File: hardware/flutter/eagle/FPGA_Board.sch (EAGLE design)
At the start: 38 parts, among them IC1 AT45DB161D-SU, U2 XC3S50AVQ100

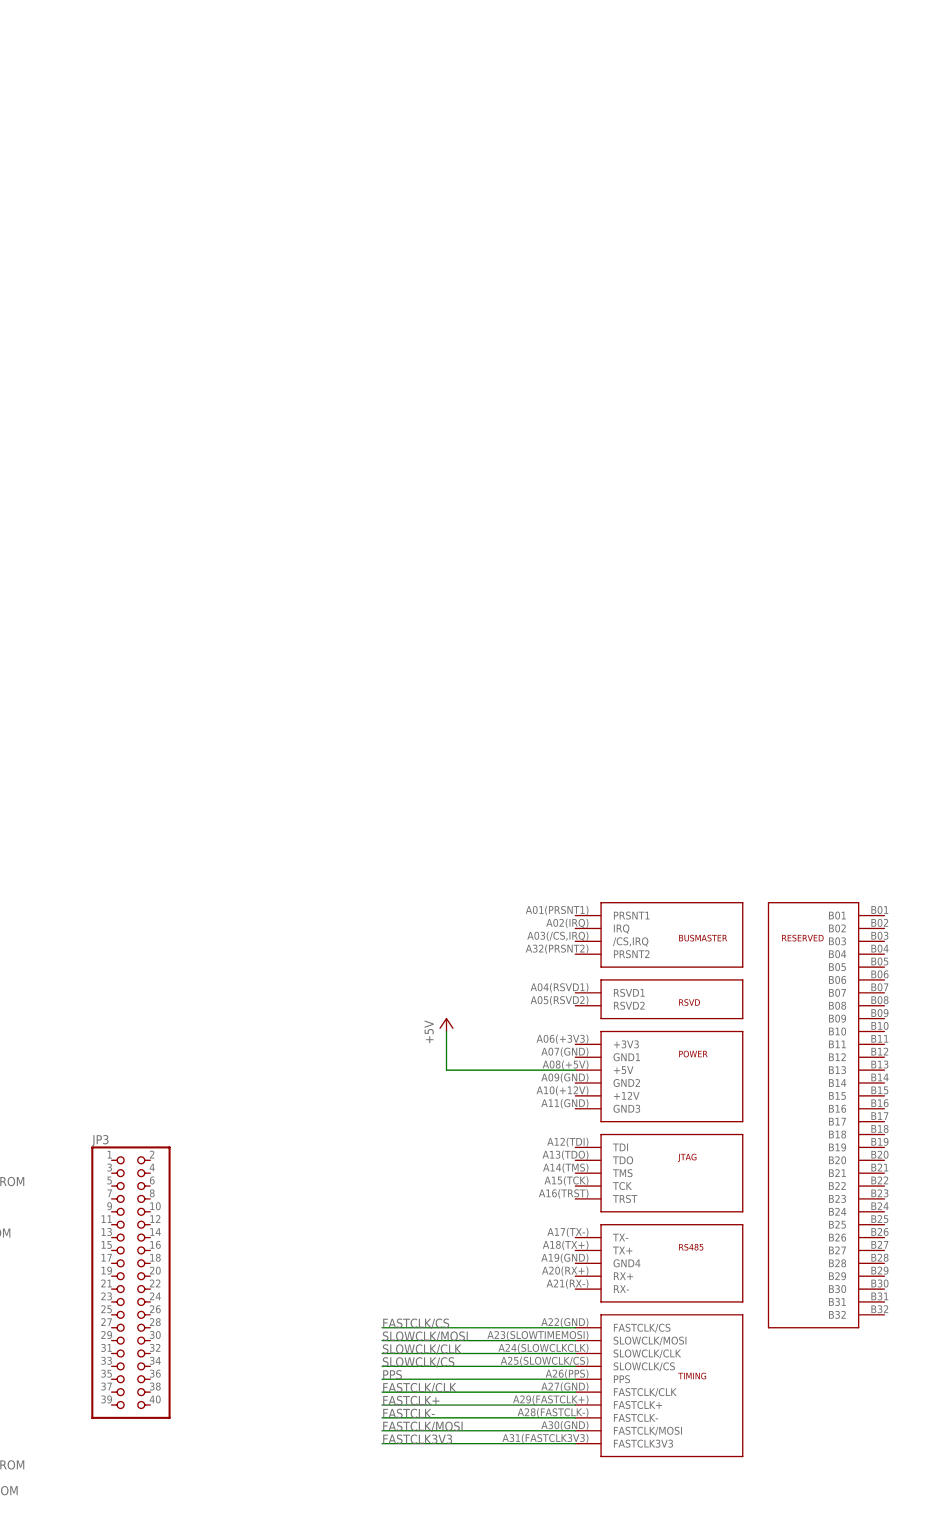
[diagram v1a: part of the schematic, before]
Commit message: added atmega8 to flutter board
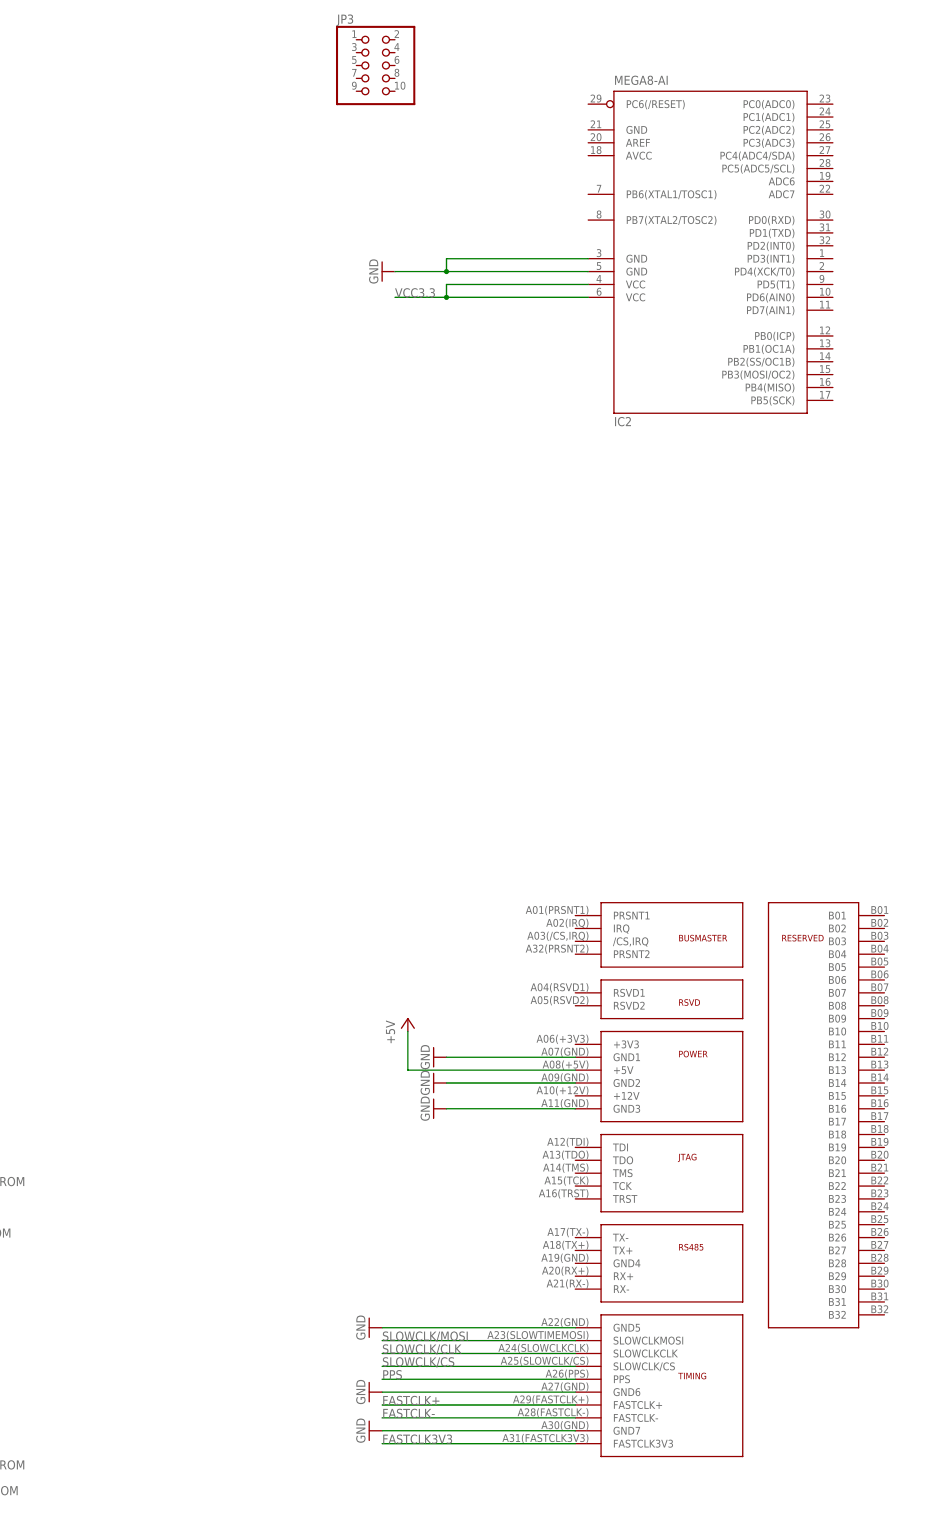
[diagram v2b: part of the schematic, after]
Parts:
- added IC2: MEGA8-AI, atmel:MEGA8-AI
- JP3: device pinhead:PINHD-2X20 -> pinhead:PINHD-2X5
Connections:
- removed net FASTCLK/CS: U$4.FASTCLK/CS
- removed net FASTCLK/MOSI: U$4.FASTCLK/MOSI
- net FASTCLK/CLK: no longer U$4.FASTCLK/CLK
- net GND: now also IC2.GND@1, IC2.GND@2, U$4.GND1, U$4.GND2, U$4.GND3, U$4.GND5, U$4.GND6, U$4.GND7
- net SLOWCLK/CLK: now also U$4.SLOWCLKCLK; no longer U$4.SLOWCLK/CLK
- net SLOWCLK/MOSI: now also U$4.SLOWCLKMOSI; no longer U$4.SLOWCLK/MOSI
- net VCC3.3: now also IC2.VCC@1, IC2.VCC@2
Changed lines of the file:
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@@
 <part name="S1" library="SparkFun" deviceset="TAC_SWITCH" device="PTH"/>
 <part name="GND15" library="supply1" deviceset="GND" device=""/>
-<part name="JP3" library="pinhead" deviceset="PINHD-2X20" device=""/>
 <part name="U$4" library="hgg" deviceset="FRIENDSHIP" device="CONNECTOR"/>
 <part name="IC1" library="atmel" deviceset="AT45DB161D" device="-SU"/>
@@
 <part name="U2" library="xilinx_devices" deviceset="XC3S50AVQ100" device=""/>
 <part name="P+7" library="supply1" deviceset="+5V" device=""/>
+<part name="IC2" library="atmel" deviceset="MEGA8" device="-AI"/>
+<part name="GND18" library="supply1" deviceset="GND" device=""/>
+<part name="GND19" library="supply1" deviceset="GND" device=""/>
+<part name="GND20" library="supply1" deviceset="GND" device=""/>
+<part name="GND21" library="supply1" deviceset="GND" device=""/>
+<part name="GND22" library="supply1" deviceset="GND" device=""/>
+<part name="GND23" library="supply1" deviceset="GND" device=""/>
+<part name="GND24" library="supply1" deviceset="GND" device=""/>
+<part name="JP3" library="pinhead" deviceset="PINHD-2X5" device=""/>
 </parts>
 <sheets>
@@
 <instance part="S1" gate="S" x="353.06" y="38.1"/>
 <instance part="GND15" gate="1" x="340.36" y="33.02"/>
-<instance part="JP3" gate="A" x="218.44" y="226.06"/>
 <instance part="U$4" gate="G$1" x="317.5" y="281.94"/>
 <instance part="IC1" gate="G$1" x="320.04" y="106.68"/>
@@
 <instance part="U2" gate="BVCCAUX" x="292.1" y="76.2"/>
 <instance part="U2" gate="BVCCINT" x="68.58" y="78.74"/>
-<instance part="P+7" gate="1" x="281.94" y="276.86"/>
+<instance part="P+7" gate="1" x="274.32" y="276.86"/>
+<instance part="IC2" gate="G$1" x="332.74" y="431.8"/>
+<instance part="GND18" gate="1" x="279.4" y="269.24" rot="R270"/>
+<instance part="GND19" gate="1" x="279.4" y="264.16" rot="R270"/>
+<instance part="GND20" gate="1" x="279.4" y="259.08" rot="R270"/>
+<instance part="GND21" gate="1" x="266.7" y="215.9" rot="R270"/>
+<instance part="GND22" gate="1" x="266.7" y="203.2" rot="R270"/>
+<instance part="GND23" gate="1" x="266.7" y="195.58" rot="R270"/>
+<instance part="GND24" gate="1" x="269.24" y="424.18" rot="R270"/>
+<instance part="JP3" gate="A" x="266.7" y="464.82"/>
 </instances>
 <busses>
@@
 <wire x1="99.06" y1="43.18" x2="99.06" y2="35.56" width="0.1524" layer="91"/>
 </segment>
+<segment>
+<pinref part="U$4" gate="G$1" pin="GND1"/>
+<wire x1="307.34" y1="269.24" x2="281.94" y2="269.24" width="0.1524" layer="91"/>
+<pinref part="GND18" gate="1" pin="GND"/>
+</segment>
+<segment>
+<pinref part="U$4" gate="G$1" pin="GND2"/>
+<wire x1="307.34" y1="264.16" x2="281.94" y2="264.16" width="0.1524" layer="91"/>
+<pinref part="GND19" gate="1" pin="GND"/>
+</segment>
+<segment>
+<pinref part="U$4" gate="G$1" pin="GND3"/>
+<wire x1="307.34" y1="259.08" x2="281.94" y2="259.08" width="0.1524" layer="91"/>
+<pinref part="GND20" gate="1" pin="GND"/>
+</segment>
+<segment>
+<pinref part="U$4" gate="G$1" pin="GND5"/>
+<wire x1="307.34" y1="215.9" x2="269.24" y2="215.9" width="0.1524" layer="91"/>
+<pinref part="GND21" gate="1" pin="GND"/>
+</segment>
+<segment>
+<pinref part="U$4" gate="G$1" pin="GND6"/>
+<wire x1="307.34" y1="203.2" x2="269.24" y2="203.2" width="0.1524" layer="91"/>
+<pinref part="GND22" gate="1" pin="GND"/>
+</segment>
+<segment>
+<pinref part="U$4" gate="G$1" pin="GND7"/>
+<wire x1="307.34" y1="195.58" x2="269.24" y2="195.58" width="0.1524" layer="91"/>
+<pinref part="GND23" gate="1" pin="GND"/>
+</segment>
+<segment>
+<pinref part="IC2" gate="G$1" pin="GND@2"/>
+<wire x1="309.88" y1="424.18" x2="281.94" y2="424.18" width="0.1524" layer="91"/>
+<pinref part="IC2" gate="G$1" pin="GND@1"/>
+<wire x1="281.94" y1="424.18" x2="271.78" y2="424.18" width="0.1524" layer="91"/>
+<wire x1="309.88" y1="426.72" x2="281.94" y2="426.72" width="0.1524" layer="91"/>
+<wire x1="281.94" y1="426.72" x2="281.94" y2="424.18" width="0.1524" layer="91"/>
+<junction x="281.94" y="424.18"/>
+<pinref part="GND24" gate="1" pin="GND"/>
+</segment>
 </net>
 <net name="+5V" class="0">
@@
 <segment>
 <pinref part="P+7" gate="1" pin="+5V"/>
-<wire x1="281.94" y1="274.32" x2="281.94" y2="266.7" width="0.1524" layer="91"/>
+<wire x1="274.32" y1="274.32" x2="274.32" y2="266.7" width="0.1524" layer="91"/>
 <pinref part="U$4" gate="G$1" pin="+5V"/>
-<wire x1="281.94" y1="266.7" x2="307.34" y2="266.7" width="0.1524" layer="91"/>
+<wire x1="274.32" y1="266.7" x2="307.34" y2="266.7" width="0.1524" layer="91"/>
 </segment>
 </net>
@@
 <wire x1="289.56" y1="139.7" x2="289.56" y2="144.78" width="0.1524" layer="91"/>
 <label x="289.56" y="139.7" size="1.778" layer="95" rot="R90"/>
+</segment>
+<segment>
+<pinref part="IC2" gate="G$1" pin="VCC@2"/>
+<wire x1="309.88" y1="419.1" x2="281.94" y2="419.1" width="0.1524" layer="91"/>
+<pinref part="IC2" gate="G$1" pin="VCC@1"/>
+<wire x1="309.88" y1="421.64" x2="281.94" y2="421.64" width="0.1524" layer="91"/>
+<wire x1="281.94" y1="421.64" x2="281.94" y2="419.1" width="0.1524" layer="91"/>
+<wire x1="281.94" y1="419.1" x2="271.78" y2="419.1" width="0.1524" layer="91"/>
+<junction x="281.94" y="419.1"/>
+<label x="271.78" y="419.1" size="1.778" layer="95"/>
 </segment>
 </net>
@@
 </segment>
 </net>
-<net name="FASTCLK/CS" class="0">
-<segment>
-<pinref part="U$4" gate="G$1" pin="FASTCLK/CS"/>
-<wire x1="307.34" y1="215.9" x2="269.24" y2="215.9" width="0.1524" layer="91"/>
-<label x="269.24" y="215.9" size="1.778" layer="95"/>
-</segment>
-</net>
 <net name="SLOWCLK/MOSI" class="0">
 <segment>
-<pinref part="U$4" gate="G$1" pin="SLOWCLK/MOSI"/>
+<pinref part="U$4" gate="G$1" pin="SLOWCLKMOSI"/>
 <wire x1="307.34" y1="213.36" x2="269.24" y2="213.36" width="0.1524" layer="91"/>
 <label x="269.24" y="213.36" size="1.778" layer="95"/>
@@
 <net name="SLOWCLK/CLK" class="0">
 <segment>
-<pinref part="U$4" gate="G$1" pin="SLOWCLK/CLK"/>
+<pinref part="U$4" gate="G$1" pin="SLOWCLKCLK"/>
 <wire x1="307.34" y1="210.82" x2="269.24" y2="210.82" width="0.1524" layer="91"/>
 <label x="269.24" y="210.82" size="1.778" layer="95"/>
@@
 <net name="FASTCLK/CLK" class="0">
 <segment>
-<pinref part="U$4" gate="G$1" pin="FASTCLK/CLK"/>
-<wire x1="307.34" y1="203.2" x2="269.24" y2="203.2" width="0.1524" layer="91"/>
-<label x="269.24" y="203.2" size="1.778" layer="95"/>
-</segment>
-<segment>
 <pinref part="U2" gate="B0" pin="IO_L02P_0/GCLK4"/>
 <wire x1="152.4" y1="447.04" x2="180.34" y2="447.04" width="0.1524" layer="91"/>
@@
 </segment>
 </net>
-<net name="FASTCLK/MOSI" class="0">
-<segment>
-<pinref part="U$4" gate="G$1" pin="FASTCLK/MOSI"/>
-<wire x1="307.34" y1="195.58" x2="269.24" y2="195.58" width="0.1524" layer="91"/>
-<label x="269.24" y="195.58" size="1.778" layer="95"/>
-</segment>
-</net>

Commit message: added RS485 level converter and 8MHz crystal to board (for uController)
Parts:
- added C11, C12: 22n, resistor:C-EUC0805
- added IC3: MAX3468CSA, maxim:MAX3468CSA
- added Q1: 8Mhz, crystal:CRYSTALHC49UP
- added R16: 1k, resistor:R-EU_M0805
- added R17: 1.6k, resistor:R-EU_M0805
- JP1: value (none) -> JTAG2
- JP2: value (none) -> JTAG1
- JP3: value (none) -> ISP
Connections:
- removed net FASTCLK/CLK: U2B0.IO_L02P_0/GCLK4, U2B0.IO_L03P_0/GCLK6
- new net N$10: IC3.A, R16.2
- new net N$11: C11.1, IC2.PB6(XTAL1/TOSC1), Q1.2
- new net N$12: C12.1, IC2.PB7(XTAL2/TOSC2), Q1.1
- new net N$5: IC3.VCC
- new net N$6: IC2.PD1(TXD), IC3.B
- new net N$9: IC2.PD0(RXD), R16.1, R17.2
- new net TRST: U$4.TRST
- new net UC_RX+: IC3.DI, U$4.TX+
- new net UC_RX-: IC3.DE, U$4.TX-
- new net UC_TX+: IC3.RO, U$4.RX+
- new net UC_TX-: IC3.RE/, U$4.RX-
- net GND: now also C11.2, C12.2, IC3.GND, R17.1, U$4.GND4
- net SLOWCLK/CLK: no longer U2B0.IO_L01P_0/VREF_0
- net SLOWCLK/CS: no longer U2B0.IO_0/GCLK11
- net SLOWCLK/MOSI: no longer U2B0.IP_0
- net TCK: now also U$4.TCK
- net TDI: now also U$4.TDI
- net TDO: now also U$4.TDO
- net TMS: now also U$4.TMS
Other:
- moved on the sheet: JP2

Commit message: organized parts of schematic by function finished routing, some power pins are not connected
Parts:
- added QG2: (no value), crystal:QG5460
- added R18, R19: 10k, resistor:R-EU_M0805
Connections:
- removed net CLOCK: QG1.OUT
- new net FPGA_SPI_CLOCK: QG1.OUT, QG2.OUT, U2B0.IO_L02P_0/GCLK4
- new net N$13: U$4.PRSNT1, U$4.PRSNT2
- new net TIMING_RESET: IC2.PC1(ADC1), R19.2, U2B0.IO_L05P_0
- new net UC_FPGA_SPI_CS: IC2.PC0(ADC0), R18.2, U2B0.IO_0/GCLK11
- new net UC_MISO: IC2.PB4(MISO), JP3.9
- new net UC_MOSI: IC2.PB3(MOSI/OC2), JP3.1, U2B0.IP_0
- new net UC_RESET: IC2.PC6(/RESET), JP3.5
- new net UC_SCK: IC2.PB5(SCK), JP3.7, U2B0.IO_L01P_0/VREF_0
- net GND: now also IC2.GND, JP3.10, JP3.4, JP3.6, JP3.8, QG2.GND, R18.1, R19.1
- net SLOWCLK/CLK: now also U2B0.IO_L03P_0/GCLK6
- net SLOWCLK/CS: now also U2B0.IO_L06P_0/VREF_0
- net SLOWCLK/MOSI: now also U2B0.IO_L06N_0/PUDC_B
- net VCC3.3: now also JP3.2, QG2.VCC
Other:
- note added: "FPGA I/O Pins"
- note added: "FPGA_SPI_Clock"
- note added: "FPGA_to_EEPROM"
- note added: "Friendship_Connector"
- note added: "JTAG"
- note added: "Microcontroller"
- note added: "Power"
- note added: "Shorten two present pins!"
- note added: "Timing_Clock"
- moved on the sheet: C1, C10, C11, C12, C2, C3, C4, C5, C6, C7, C8, C9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

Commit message: connected all the signals to wires just gps module is missing on the board
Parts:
- added C13, C14, C15, C16, C18, C19, C20, C21, C22, C23, C24: (no value), resistor:C-EUC0603
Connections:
- net GND: now also C13.2, C14.2, C15.2, C16.2, C18.2, C19.2, C20.2, C21.2, C22.2, C23.2, C24.2
- net VCC1.2: now also C18.1, C19.1, C20.1, C24.1
- net VCC2.5: now also C21.1, C22.1, C23.1
- net VCC3.3: now also C13.1, C14.1, C15.1, C16.1, IC2.AVCC
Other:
- moved on the sheet: C1, C10, C2, C3, C4, C5, C6, C7, C8, C9, LED1, R1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

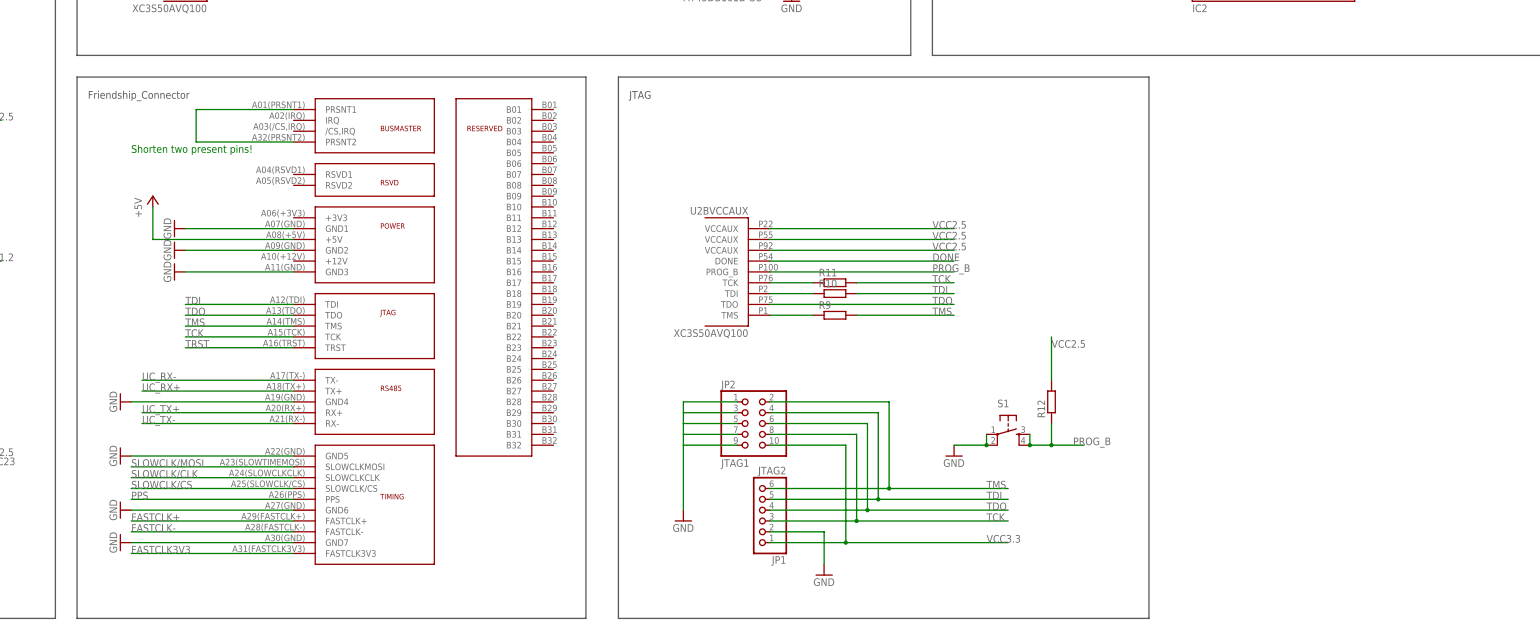
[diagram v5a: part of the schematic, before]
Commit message: applied changed in hgg.lbr to the board, added ground planes
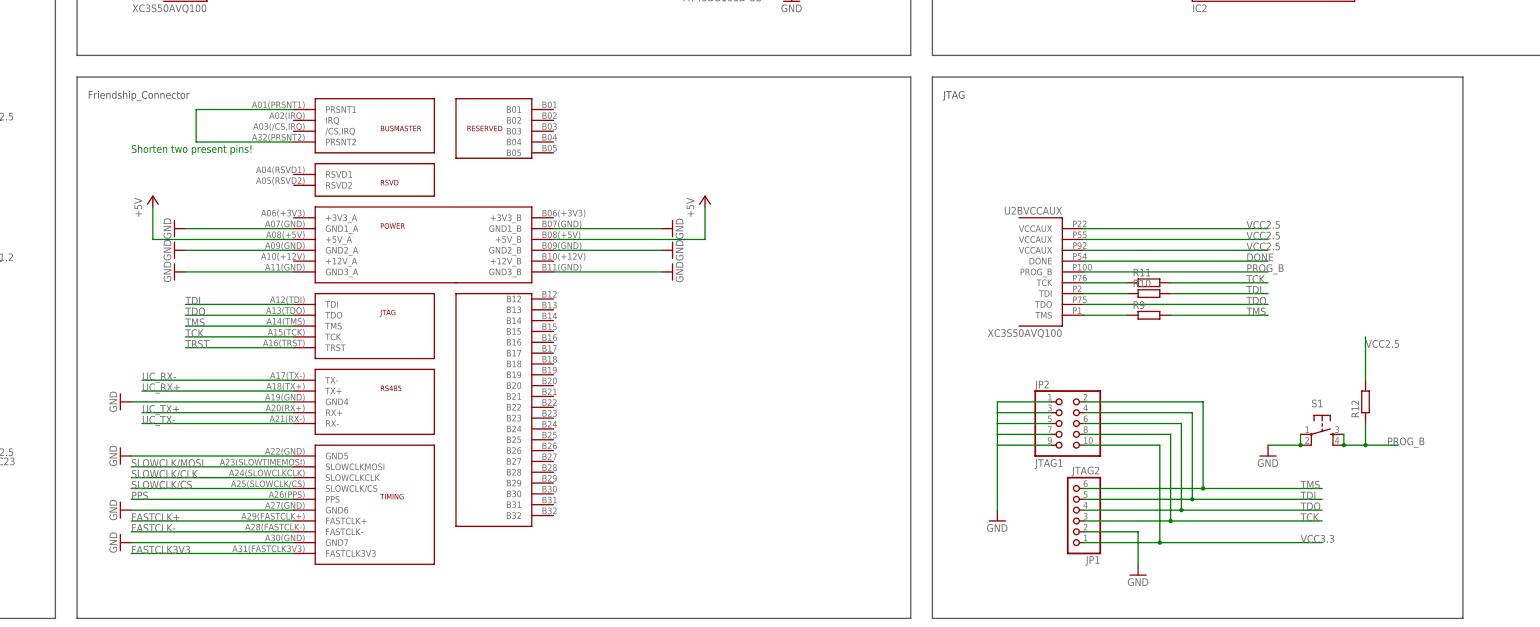
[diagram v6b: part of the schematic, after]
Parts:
- added U$5: HGG_LOGO, hgg:HGG_LOGO
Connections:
- net +5V: now also U$4.+5V_A, U$4.+5V_B; no longer U$4.+5V
- net GND: now also U$4.GND1_A, U$4.GND1_B, U$4.GND2_A, U$4.GND2_B, U$4.GND3_A, U$4.GND3_B; no longer U$4.GND1, U$4.GND2, U$4.GND3
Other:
- moved on the sheet: JP1, JP2, R10, R11, R12, R9, S1, U2BVCCAUX
